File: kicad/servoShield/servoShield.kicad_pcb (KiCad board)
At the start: 2 copper layers, 52.8 x 53.8 mm, 11 parts, among them M1 Motor_Servo, M2 Motor_Servo, M3 Motor_Servo, M4 Motor_Servo, M5 Motor_Servo, M6 Motor_Servo, M7 Motor_Servo, M8 Motor_Servo

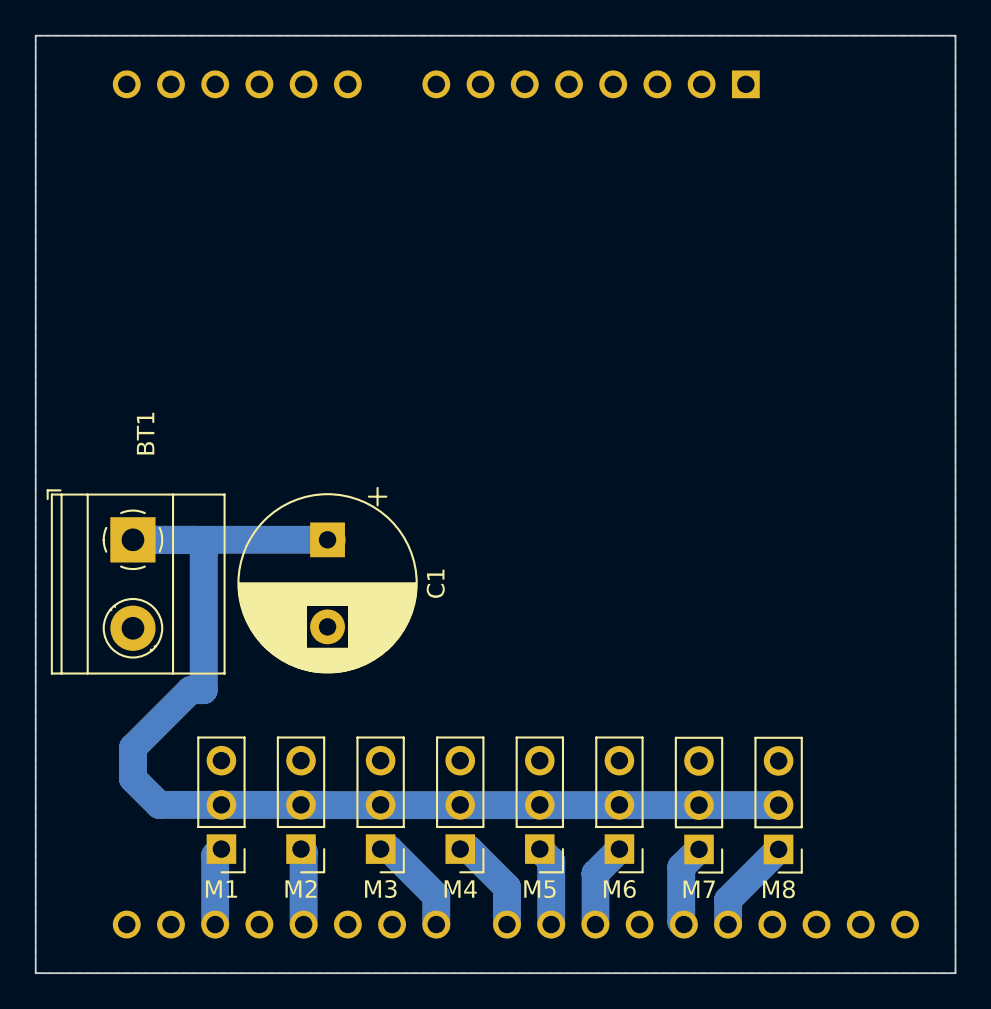
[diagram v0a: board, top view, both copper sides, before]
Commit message: created custom pads for arduino shield
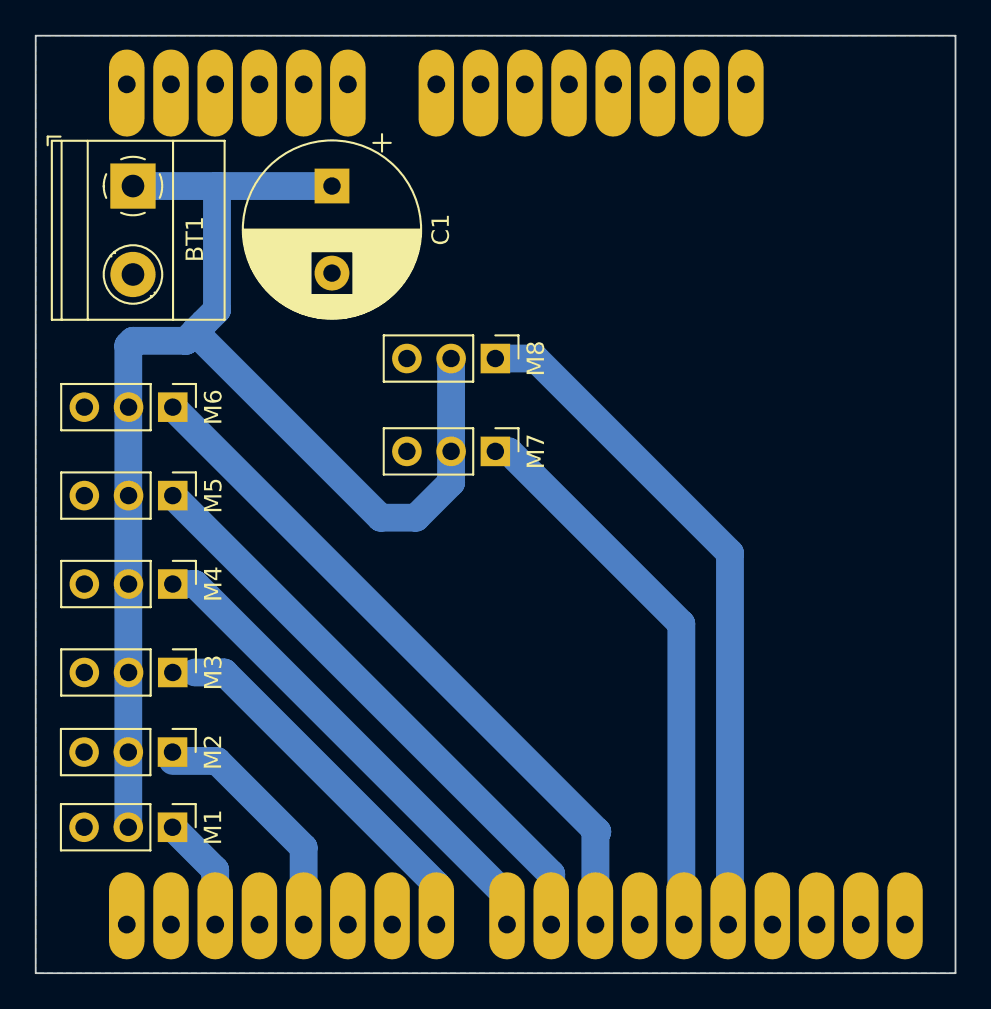
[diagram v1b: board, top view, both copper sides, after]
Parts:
- moved M6 36.1 mm to (118.1, 48.3), turned to -90 degrees
- moved M8 32.6 mm to (136.6, 45.5), turned to -90 degrees
- moved M5 29.3 mm to (118.1, 53.3), turned to -90 degrees
- moved M7 25.7 mm to (136.6, 50.8), turned to -90 degrees
- moved M4 22.5 mm to (118.1, 58.4), turned to -90 degrees
- moved C1 20.3 mm to (127.3, 35.6)
- moved BT1 20.3 mm to (115.8, 35.6)
- moved M3 15.7 mm to (118.1, 63.5), turned to -90 degrees
- moved M2 9.25 mm to (118.1, 68.1), turned to -90 degrees
- moved M1 3.08 mm to (118.1, 72.4), turned to -90 degrees
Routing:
- net Net-(A1-Pad25): track 4.90 -> 39.9 mm
- net Net-(A1-Pad28): track 5.52 -> 39.5 mm
- net Net-(A1-Pad24): track 4.60 -> 33.6 mm
- net Net-(A1-Pad27): track 4.80 -> 32.1 mm
- net Net-(A1-Pad23): track 5.73 -> 28.3 mm
- net Net-(A1-Pad22): track 5.95 -> 21.2 mm
- net Net-(BT1-Pad1): track 68.8 -> 79.3 mm
- net Net-(A1-Pad19): track 4.40 -> 14.0 mm
- net Net-(A1-Pad17): track 4.48 -> 6.60 mm
